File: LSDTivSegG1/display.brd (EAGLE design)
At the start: 160 x 100 mm, 93 parts, among them IC1 MEGA8-P, IC2 MAX232, IC3 PCF8574P, IC4 PCF8574P, IC5 PCF8574P, IC6 PCF8574P

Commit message: changed resistor packages on sheet 1
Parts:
- added U$2: PCB, lsd2016:BOARD
- R1, R10, R11, R36, R37, R38, R39: device rcl:0207/2V -> rcl:0207/10
- moved C3 209.0 mm to (78.7, 43.2), flipped to the bottom, turned to 270 degrees
- moved C2 198.0 mm to (73.7, 43.2), turned to 270 degrees
- moved C8 188.7 mm to (43.2, 22.9), turned to 90 degrees
- moved Q1 184.0 mm to (76.2, 49.5)
- moved C1 171.9 mm to (54.6, 49.5), turned to 270 degrees
- moved IC1 169.1 mm to (71.1, 58.4)
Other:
- board size 160 x 100 mm -> 150 x 100 mm

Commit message: exported schematic as PDF
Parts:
- moved R10 193.3 mm to (57.1, 69.8), turned to 90 degrees
- moved R1 128.9 mm to (50.8, 49.5), turned to 270 degrees
- moved R11 113.8 mm to (53.3, 69.8), turned to 90 degrees
- moved C8 36.8 mm to (68.6, 49.5)
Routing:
- added copper zone on layer 1, net GND

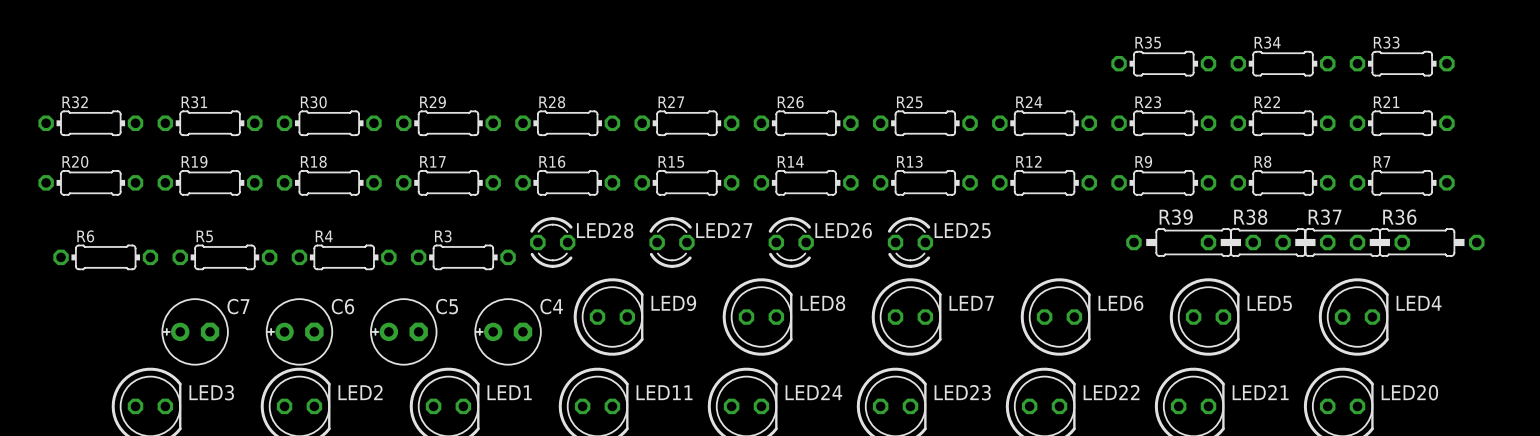
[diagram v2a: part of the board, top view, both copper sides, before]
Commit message: added values for all the parts in schematic added some datasheets
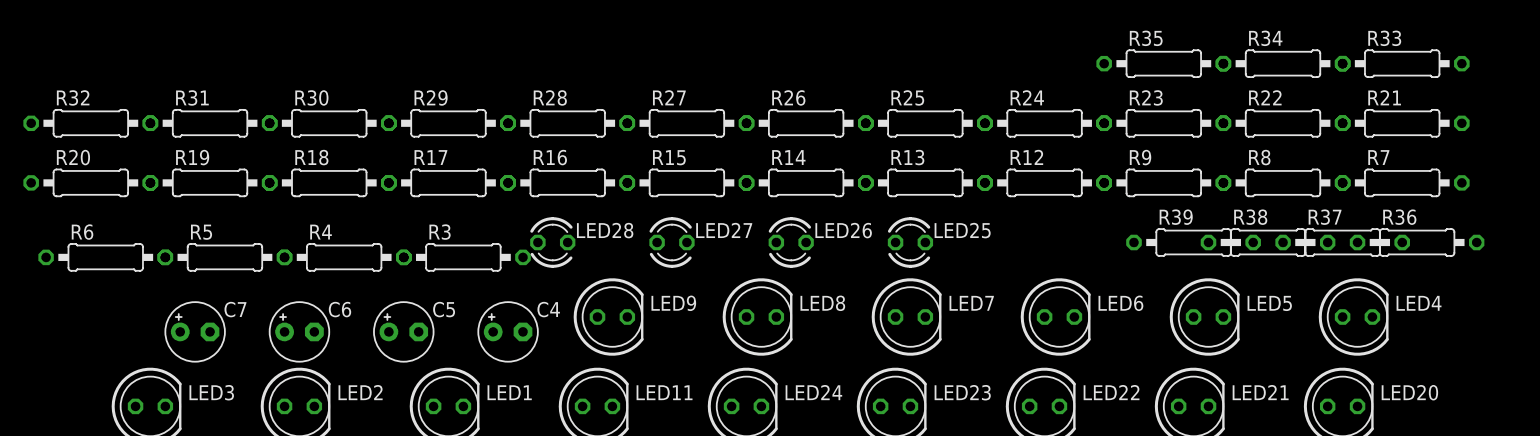
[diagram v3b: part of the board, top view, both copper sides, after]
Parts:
- C4, C5, C6, C7: value (none) -> 1uF; device rcl:E2,5-6E -> rcl:E2,5-5
- LED1, LED13, LED14, LED15, LED16, LED17, LED18, LED2, LED26, LED3, LED4, LED5, LED6: value (none) -> green
- LED10, LED19, LED20, LED21, LED22, LED27, LED7, LED8, LED9: value (none) -> yellow
- LED11, LED12, LED23, LED24, LED28: value (none) -> red
- LED25: value (none) -> blue
- R12, R13, R14, R15, R16, R17, R18, R19, R20, R21, R24, R25, R26, R27, R28, R29, R30, R31, R32, R33: value (none) -> 100R; device rcl:0204/7 -> rcl:0207/10
- R2: value (none) -> 10k
- R22, R23, R34, R35: value (none) -> 150R; device rcl:0204/7 -> rcl:0207/10
- R3, R4, R5: device rcl:0204/7 -> rcl:0207/10
- R36, R37: value 4k7 -> 100R
- R38: value 4k7 -> 220R
- R39: value 4k7 -> 150R
- R6, R7, R8, R9: value (none) -> 10k; device rcl:0204/7 -> rcl:0207/10

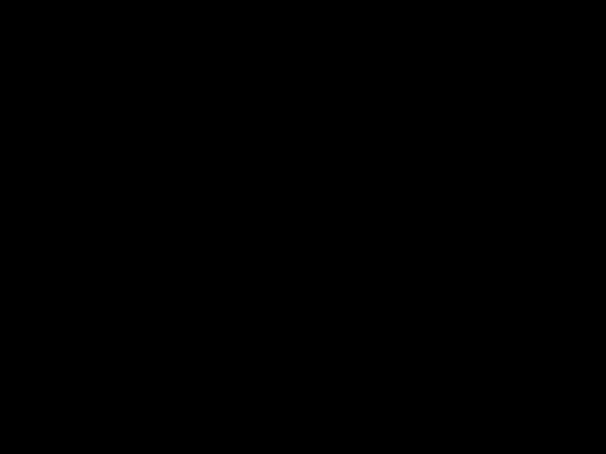
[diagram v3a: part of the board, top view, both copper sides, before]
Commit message: added jumper to interrupt VCC via RS232 to debug
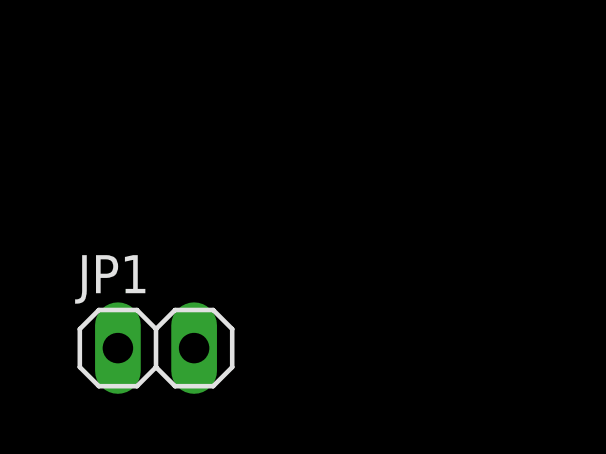
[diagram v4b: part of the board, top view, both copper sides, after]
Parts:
- added JP1: (no value), pinhead:1X02
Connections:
- new net N$48: JP1.1, X1.9
- net +5V: now also JP1.2; no longer X1.9
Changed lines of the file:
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@@
 </element>
 <element name="U$2" library="lsd2016" package="BOARD" value="PCB" x="0" y="0"/>
+<element name="JP1" library="pinhead" library_urn="urn:adsk.eagle:library:325" package="1X02" package3d_urn="urn:adsk.eagle:package:22435/2" value="" x="-132.08" y="-5.08"/>
 </elements>
 <signals>
@@
 <contactref element="R3" pad="1"/>
 <contactref element="R5" pad="2"/>
-<contactref element="X1" pad="9"/>
 <contactref element="C6" pad="-"/>
 <contactref element="R12" pad="2"/>
@@
 <contactref element="IC6" pad="2"/>
 <contactref element="IC6" pad="1"/>
+<contactref element="JP1" pad="2"/>
 <wire x1="72.39" y1="62.23" x2="74.93" y2="62.23" width="0" layer="19" extent="1-1"/>
 <wire x1="69.85" y1="54.61" x2="72.39" y2="62.23" width="0" layer="19" extent="1-1"/>
@@
 <wire x1="57.15" y1="74.93" x2="72.39" y2="62.23" width="0" layer="19" extent="1-1"/>
 <wire x1="53.34" y1="74.93" x2="57.15" y2="74.93" width="0" layer="19" extent="1-1"/>
-<wire x1="-25.0952" y1="69.85" x2="53.34" y2="74.93" width="0" layer="19" extent="1-1"/>
-<wire x1="-33.02" y1="96.52" x2="-25.0952" y2="69.85" width="0" layer="19" extent="1-1"/>
+<wire x1="-33.02" y1="96.52" x2="53.34" y2="74.93" width="0" layer="19" extent="1-1"/>
 <wire x1="-57.15" y1="96.52" x2="-33.02" y2="96.52" width="0" layer="19" extent="1-1"/>
 <wire x1="-57.15" y1="88.9" x2="-57.15" y2="96.52" width="0" layer="19" extent="1-1"/>
@@
 <wire x1="-114.3" y1="137.16" x2="-113.03" y2="130.81" width="0" layer="19" extent="1-1"/>
 <wire x1="-114.3" y1="142.24" x2="-114.3" y2="137.16" width="0" layer="19" extent="1-1"/>
-<wire x1="-104.14" y1="142.24" x2="-114.3" y2="142.24" width="0" layer="19" extent="1-1"/>
-<wire x1="-104.14" y1="137.16" x2="-104.14" y2="142.24" width="0" layer="19" extent="1-1"/>
-<wire x1="-102.87" y1="130.81" x2="-104.14" y2="137.16" width="0" layer="19" extent="1-1"/>
-<wire x1="-93.98" y1="137.16" x2="-102.87" y2="130.81" width="0" layer="19" extent="1-1"/>
-<wire x1="-93.98" y1="142.24" x2="-93.98" y2="137.16" width="0" layer="19" extent="1-1"/>
+<wire x1="-102.87" y1="130.81" x2="-110.49" y2="124.46" width="0" layer="19" extent="1-1"/>
+<wire x1="-104.14" y1="137.16" x2="-102.87" y2="130.81" width="0" layer="19" extent="1-1"/>
+<wire x1="-104.14" y1="142.24" x2="-104.14" y2="137.16" width="0" layer="19" extent="1-1"/>
+<wire x1="-93.98" y1="142.24" x2="-104.14" y2="142.24" width="0" layer="19" extent="1-1"/>
+<wire x1="-93.98" y1="137.16" x2="-93.98" y2="142.24" width="0" layer="19" extent="1-1"/>
 <wire x1="-83.82" y1="142.24" x2="-93.98" y2="142.24" width="0" layer="19" extent="1-1"/>
 <wire x1="-83.82" y1="137.16" x2="-83.82" y2="142.24" width="0" layer="19" extent="1-1"/>
@@
 <wire x1="-43.18" y1="142.24" x2="-53.34" y2="142.24" width="0" layer="19" extent="1-1"/>
 <wire x1="-43.18" y1="137.16" x2="-43.18" y2="142.24" width="0" layer="19" extent="1-1"/>
-<wire x1="-43.18" y1="137.16" x2="-43.18" y2="137.16" width="0" layer="19" extent="1-1"/>
-<wire x1="-33.02" y1="142.24" x2="-43.18" y2="137.16" width="0" layer="19" extent="1-1"/>
+<wire x1="-33.02" y1="142.24" x2="-43.18" y2="142.24" width="0" layer="19" extent="1-1"/>
 <wire x1="-33.02" y1="147.32" x2="-33.02" y2="142.24" width="0" layer="19" extent="1-1"/>
 <wire x1="-33.02" y1="137.16" x2="-33.02" y2="142.24" width="0" layer="19" extent="1-1"/>
-<wire x1="-22.86" y1="142.24" x2="-33.02" y2="137.16" width="0" layer="19" extent="1-1"/>
-<wire x1="-22.86" y1="147.32" x2="-22.86" y2="142.24" width="0" layer="19" extent="1-1"/>
+<wire x1="-22.86" y1="147.32" x2="-33.02" y2="147.32" width="0" layer="19" extent="1-1"/>
+<wire x1="-22.86" y1="142.24" x2="-22.86" y2="147.32" width="0" layer="19" extent="1-1"/>
 <wire x1="-22.86" y1="137.16" x2="-22.86" y2="142.24" width="0" layer="19" extent="1-1"/>
-<wire x1="-12.7" y1="142.24" x2="-22.86" y2="137.16" width="0" layer="19" extent="1-1"/>
-<wire x1="-12.7" y1="147.32" x2="-12.7" y2="142.24" width="0" layer="19" extent="1-1"/>
+<wire x1="-12.7" y1="147.32" x2="-22.86" y2="147.32" width="0" layer="19" extent="1-1"/>
+<wire x1="-12.7" y1="142.24" x2="-12.7" y2="147.32" width="0" layer="19" extent="1-1"/>
 <wire x1="-124.46" y1="142.24" x2="-114.3" y2="142.24" width="0" layer="19" extent="1-1"/>
 <wire x1="-124.46" y1="137.16" x2="-124.46" y2="142.24" width="0" layer="19" extent="1-1"/>
 <wire x1="-133.35" y1="130.81" x2="-124.46" y2="137.16" width="0" layer="19" extent="1-1"/>
 <wire x1="-99.06" y1="58.42" x2="-102.87" y2="88.9" width="0" layer="19" extent="1-1"/>
+<wire x1="-130.81" y1="-5.08" x2="-99.06" y2="58.42" width="0" layer="19" extent="1-1"/>
 </signal>
 <signal name="N$2">
@@
 <wire x1="-97.79" y1="96.52" x2="-33.02" y2="137.16" width="0" layer="19" extent="1-1"/>
 </signal>
+<signal name="N$48">
+<contactref element="X1" pad="9"/>
+<contactref element="JP1" pad="1"/>
+<wire x1="-25.0952" y1="69.85" x2="-133.35" y2="-5.08" width="0" layer="19" extent="1-1"/>
+</signal>
 </signals>

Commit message: added jumper to rs232 connector to interrupt 5V supply
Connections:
- net GND: now also C7.+; no longer C7.-
- net N$8: now also C7.-; no longer C7.+
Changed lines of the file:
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@@
 <contactref element="X1" pad="5"/>
 <contactref element="X1" pad="1"/>
-<contactref element="C7" pad="-"/>
 <contactref element="S8" pad="1"/>
 <contactref element="S7" pad="1"/>
@@
 <vertex x="0" y="0"/>
 </polygon>
-<wire x1="-27.94" y1="132.08" x2="-21.59" y2="132.08" width="0" layer="19" extent="1-1"/>
-<wire x1="-34.29" y1="132.08" x2="-27.94" y2="132.08" width="0" layer="19" extent="1-1"/>
-<wire x1="-40.64" y1="132.08" x2="-34.29" y2="132.08" width="0" layer="19" extent="1-1"/>
-<wire x1="-21.0312" y1="103.8606" x2="-21.59" y2="132.08" width="0" layer="19" extent="1-1"/>
-<wire x1="-24.6888" y1="103.8606" x2="-21.0312" y2="103.8606" width="0" layer="19" extent="1-1"/>
+<contactref element="C7" pad="+"/>
+<wire x1="72.39" y1="54.61" x2="69.85" y2="62.23" width="0" layer="19" extent="1-1"/>
+<wire x1="68.58" y1="50.8" x2="72.39" y2="54.61" width="0" layer="19" extent="1-1"/>
+<wire x1="73.66" y1="41.91" x2="68.58" y2="50.8" width="0" layer="19" extent="1-1"/>
+<wire x1="78.74" y1="41.91" x2="73.66" y2="41.91" width="0" layer="19" extent="1-1"/>
+<wire x1="54.61" y1="48.26" x2="68.58" y2="50.8" width="0" layer="19" extent="1-1"/>
+<wire x1="-23.7236" y1="67.31" x2="54.61" y2="48.26" width="0" layer="19" extent="1-1"/>
+<wire x1="-34.6964" y1="67.31" x2="-23.7236" y2="67.31" width="0" layer="19" extent="1-1"/>
+<wire x1="-53.34" y1="62.23" x2="-34.6964" y2="67.31" width="0" layer="19" extent="1-1"/>
+<wire x1="-63.5" y1="58.42" x2="-53.34" y2="62.23" width="0" layer="19" extent="1-1"/>
+<wire x1="-64.77" y1="64.77" x2="-63.5" y2="58.42" width="0" layer="19" extent="1-1"/>
+<wire x1="-67.31" y1="64.77" x2="-64.77" y2="64.77" width="0" layer="19" extent="1-1"/>
+<wire x1="-69.85" y1="64.77" x2="-67.31" y2="64.77" width="0" layer="19" extent="1-1"/>
+<wire x1="-72.39" y1="64.77" x2="-69.85" y2="64.77" width="0" layer="19" extent="1-1"/>
+<wire x1="-33.02" y1="88.9" x2="-34.6964" y2="67.31" width="0" layer="19" extent="1-1"/>
+<wire x1="-30.48" y1="88.9" x2="-33.02" y2="88.9" width="0" layer="19" extent="1-1"/>
+<wire x1="-27.94" y1="88.9" x2="-30.48" y2="88.9" width="0" layer="19" extent="1-1"/>
+<wire x1="-39.37" y1="88.9" x2="-33.02" y2="88.9" width="0" layer="19" extent="1-1"/>
+<wire x1="-15.24" y1="88.9" x2="-27.94" y2="88.9" width="0" layer="19" extent="1-1"/>
+<wire x1="-52.07" y1="88.9" x2="-39.37" y2="88.9" width="0" layer="19" extent="1-1"/>
+<wire x1="-54.61" y1="88.9" x2="-52.07" y2="88.9" width="0" layer="19" extent="1-1"/>
+<wire x1="-63.5" y1="88.9" x2="-54.61" y2="88.9" width="0" layer="19" extent="1-1"/>
+<wire x1="-76.2" y1="88.9" x2="-63.5" y2="88.9" width="0" layer="19" extent="1-1"/>
+<wire x1="-81.28" y1="88.9" x2="-76.2" y2="88.9" width="0" layer="19" extent="1-1"/>
+<wire x1="-87.63" y1="88.9" x2="-81.28" y2="88.9" width="0" layer="19" extent="1-1"/>
+<wire x1="-100.33" y1="88.9" x2="-87.63" y2="88.9" width="0" layer="19" extent="1-1"/>
+<wire x1="-51.5112" y1="103.8606" x2="-52.07" y2="88.9" width="0" layer="19" extent="1-1"/>
+<wire x1="-55.1688" y1="103.8606" x2="-51.5112" y2="103.8606" width="0" layer="19" extent="1-1"/>
+<wire x1="-45.0088" y1="103.8606" x2="-51.5112" y2="103.8606" width="0" layer="19" extent="1-1"/>
+<wire x1="-41.3512" y1="103.8606" x2="-45.0088" y2="103.8606" width="0" layer="19" extent="1-1"/>
+<wire x1="-34.8488" y1="103.8606" x2="-41.3512" y2="103.8606" width="0" layer="19" extent="1-1"/>
+<wire x1="-31.1912" y1="103.8606" x2="-34.8488" y2="103.8606" width="0" layer="19" extent="1-1"/>
+<wire x1="-24.6888" y1="103.8606" x2="-31.1912" y2="103.8606" width="0" layer="19" extent="1-1"/>
+<wire x1="-21.0312" y1="103.8606" x2="-24.6888" y2="103.8606" width="0" layer="19" extent="1-1"/>
 <wire x1="-14.5288" y1="103.8606" x2="-21.0312" y2="103.8606" width="0" layer="19" extent="1-1"/>
-<wire x1="-31.1912" y1="103.8606" x2="-24.6888" y2="103.8606" width="0" layer="19" extent="1-1"/>
-<wire x1="-34.8488" y1="103.8606" x2="-31.1912" y2="103.8606" width="0" layer="19" extent="1-1"/>
-<wire x1="-41.3512" y1="103.8606" x2="-34.8488" y2="103.8606" width="0" layer="19" extent="1-1"/>
-<wire x1="-45.0088" y1="103.8606" x2="-41.3512" y2="103.8606" width="0" layer="19" extent="1-1"/>
-<wire x1="-51.5112" y1="103.8606" x2="-45.0088" y2="103.8606" width="0" layer="19" extent="1-1"/>
-<wire x1="-55.1688" y1="103.8606" x2="-51.5112" y2="103.8606" width="0" layer="19" extent="1-1"/>
 <wire x1="-61.6712" y1="103.8606" x2="-55.1688" y2="103.8606" width="0" layer="19" extent="1-1"/>
 <wire x1="-65.3288" y1="103.8606" x2="-61.6712" y2="103.8606" width="0" layer="19" extent="1-1"/>
@@
 <wire x1="-85.6488" y1="103.8606" x2="-81.9912" y2="103.8606" width="0" layer="19" extent="1-1"/>
 <wire x1="-92.1512" y1="103.8606" x2="-85.6488" y2="103.8606" width="0" layer="19" extent="1-1"/>
-<wire x1="-52.07" y1="88.9" x2="-51.5112" y2="103.8606" width="0" layer="19" extent="1-1"/>
-<wire x1="-54.61" y1="88.9" x2="-52.07" y2="88.9" width="0" layer="19" extent="1-1"/>
-<wire x1="-63.5" y1="88.9" x2="-54.61" y2="88.9" width="0" layer="19" extent="1-1"/>
-<wire x1="-39.37" y1="88.9" x2="-52.07" y2="88.9" width="0" layer="19" extent="1-1"/>
-<wire x1="-33.02" y1="88.9" x2="-39.37" y2="88.9" width="0" layer="19" extent="1-1"/>
-<wire x1="-30.48" y1="88.9" x2="-33.02" y2="88.9" width="0" layer="19" extent="1-1"/>
-<wire x1="-27.94" y1="88.9" x2="-30.48" y2="88.9" width="0" layer="19" extent="1-1"/>
-<wire x1="-15.24" y1="88.9" x2="-27.94" y2="88.9" width="0" layer="19" extent="1-1"/>
-<wire x1="-76.2" y1="88.9" x2="-63.5" y2="88.9" width="0" layer="19" extent="1-1"/>
-<wire x1="-81.28" y1="88.9" x2="-76.2" y2="88.9" width="0" layer="19" extent="1-1"/>
-<wire x1="-87.63" y1="88.9" x2="-81.28" y2="88.9" width="0" layer="19" extent="1-1"/>
-<wire x1="-100.33" y1="88.9" x2="-87.63" y2="88.9" width="0" layer="19" extent="1-1"/>
-<wire x1="-34.6964" y1="67.31" x2="-33.02" y2="88.9" width="0" layer="19" extent="1-1"/>
-<wire x1="-23.7236" y1="67.31" x2="-34.6964" y2="67.31" width="0" layer="19" extent="1-1"/>
-<wire x1="-53.34" y1="62.23" x2="-34.6964" y2="67.31" width="0" layer="19" extent="1-1"/>
-<wire x1="-63.5" y1="58.42" x2="-53.34" y2="62.23" width="0" layer="19" extent="1-1"/>
-<wire x1="-64.77" y1="64.77" x2="-63.5" y2="58.42" width="0" layer="19" extent="1-1"/>
-<wire x1="-67.31" y1="64.77" x2="-64.77" y2="64.77" width="0" layer="19" extent="1-1"/>
-<wire x1="-69.85" y1="64.77" x2="-67.31" y2="64.77" width="0" layer="19" extent="1-1"/>
-<wire x1="-72.39" y1="64.77" x2="-69.85" y2="64.77" width="0" layer="19" extent="1-1"/>
 <wire x1="-127" y1="96.52" x2="-100.33" y2="88.9" width="0" layer="19" extent="1-1"/>
-<wire x1="-119.38" y1="124.46" x2="-127" y2="96.52" width="0" layer="19" extent="1-1"/>
-<wire x1="-102.87" y1="130.81" x2="-119.38" y2="124.46" width="0" layer="19" extent="1-1"/>
+<wire x1="-21.59" y1="132.08" x2="-21.0312" y2="103.8606" width="0" layer="19" extent="1-1"/>
+<wire x1="-27.94" y1="132.08" x2="-21.59" y2="132.08" width="0" layer="19" extent="1-1"/>
+<wire x1="-34.29" y1="132.08" x2="-27.94" y2="132.08" width="0" layer="19" extent="1-1"/>
+<wire x1="-40.64" y1="132.08" x2="-34.29" y2="132.08" width="0" layer="19" extent="1-1"/>
+<wire x1="-121.92" y1="124.46" x2="-127" y2="96.52" width="0" layer="19" extent="1-1"/>
+<wire x1="-102.87" y1="130.81" x2="-121.92" y2="124.46" width="0" layer="19" extent="1-1"/>
 <wire x1="-101.6" y1="58.42" x2="-72.39" y2="64.77" width="0" layer="19" extent="1-1"/>
-<wire x1="54.61" y1="48.26" x2="-23.7236" y2="67.31" width="0" layer="19" extent="1-1"/>
 </signal>
 <signal name="RESET">
@@
 <wire x1="-92.71" y1="124.46" x2="-124.46" y2="88.9" width="0" layer="19" extent="1-1"/>
 </signal>
-<signal name="N$8">
-<contactref element="IC2" pad="6"/>
-<contactref element="C7" pad="+"/>
-<wire x1="-121.92" y1="124.46" x2="-116.84" y2="88.9" width="0" layer="19" extent="1-1"/>
-</signal>
 <signal name="N$7">
 <contactref element="IC2" pad="2"/>
@@
 <wire x1="-25.0952" y1="69.85" x2="-133.35" y2="-5.08" width="0" layer="19" extent="1-1"/>
 </signal>
+<signal name="N$8">
+<contactref element="IC2" pad="6"/>
+<contactref element="C7" pad="-"/>
+<wire x1="-119.38" y1="124.46" x2="-116.84" y2="88.9" width="0" layer="19" extent="1-1"/>
+</signal>
 </signals>
